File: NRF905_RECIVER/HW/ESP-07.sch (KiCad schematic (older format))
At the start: 2 parts, among them U3 ESP-07

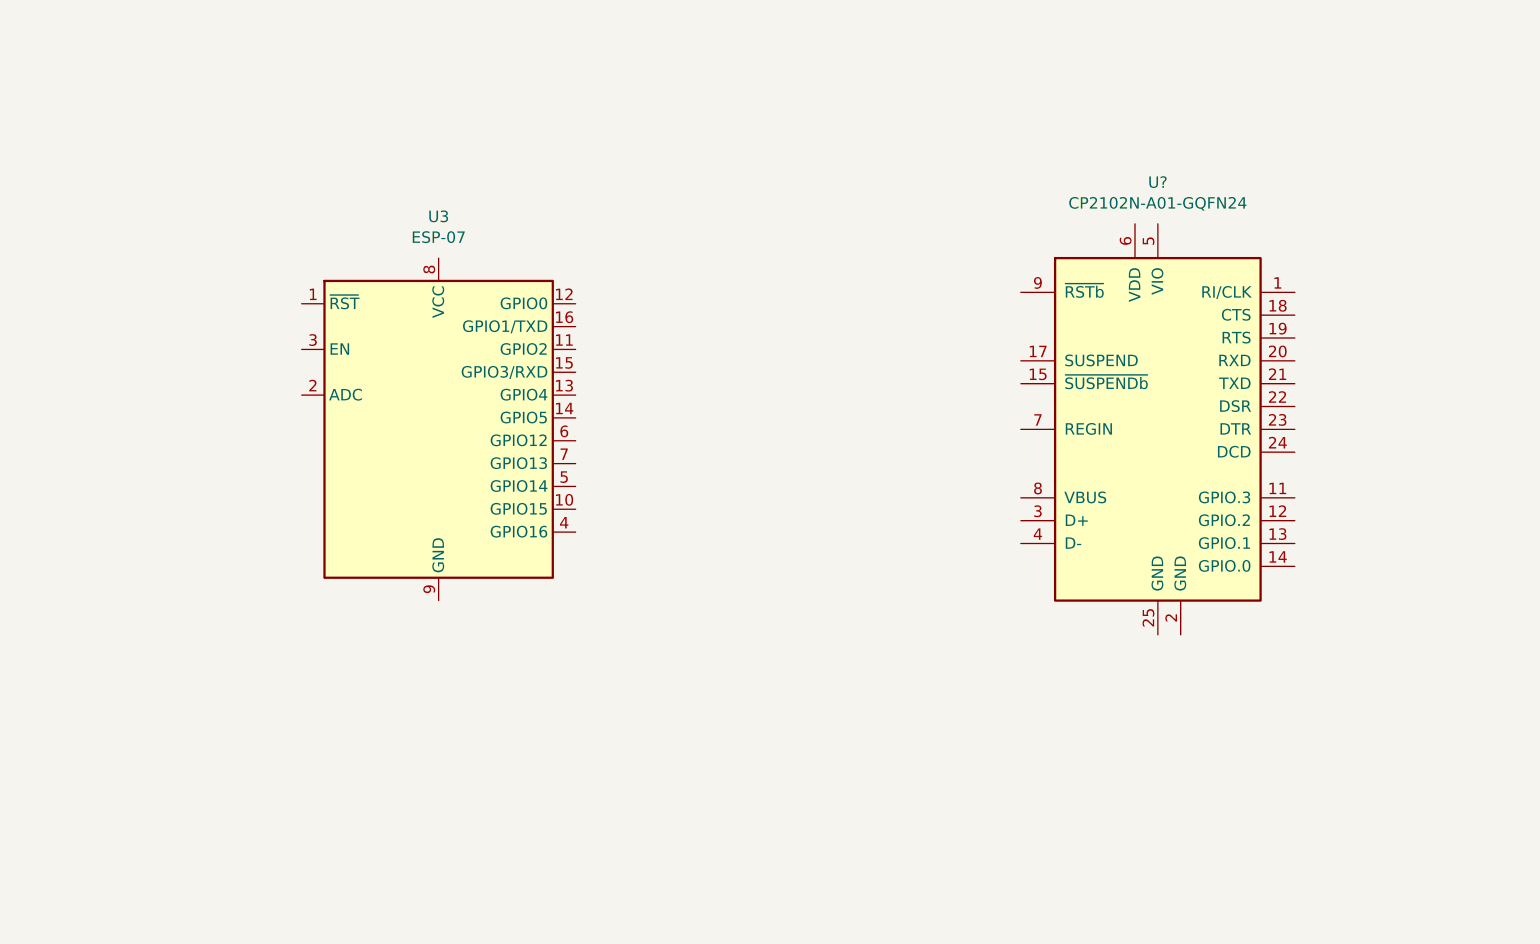
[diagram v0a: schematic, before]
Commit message: Изменена структура проека. Добавлен шаблон проекта для ESP32. Изменение в схемотехнике WIFI модуль с ESP-07 изменени на ESP32 WROVER-IB
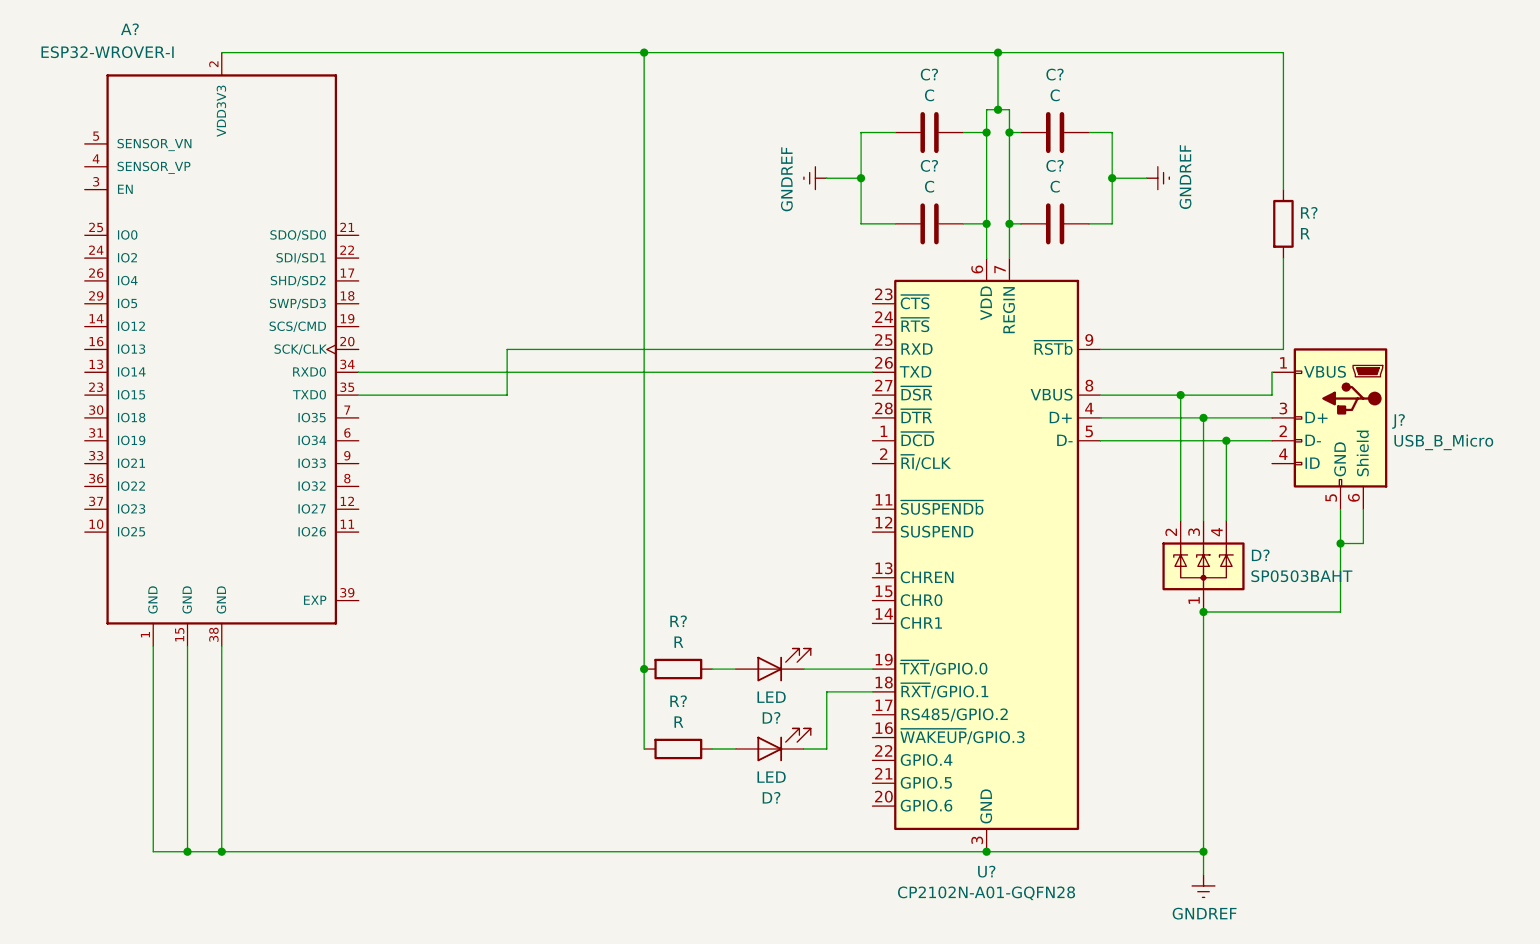
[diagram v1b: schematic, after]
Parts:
- removed U3: ESP-07, RF_Module:ESP-07, symbol RF_Module:ESP-07
- removed U?: CP2102N-A01-GQFN24, Package_DFN_QFN:QFN-24-1EP_4x4mm_P0.5mm_EP2.6x2.6mm, symbol Interface_USB:CP2102N-A01-GQFN24
- added A?: ESP32-WROVER-I, XCVR_ESP32-WROVER-I, symbol ESP32-WROVER-I:ESP32-WROVER-I
- added C? (x4): C, symbol Device:C
- added D?: SP0503BAHT, Package_TO_SOT_SMD:SOT-143, symbol Power_Protection:SP0503BAHT
- added D? (x2): LED, symbol Device:LED
- added J?: USB_B_Micro, symbol Connector:USB_B_Micro
- added R? (x3): R, symbol Device:R
- added U?: CP2102N-A01-GQFN28, Package_DFN_QFN:QFN-28-1EP_5x5mm_P0.5mm_EP3.35x3.35mm, symbol Interface_USB:CP2102N-A01-GQFN28
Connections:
- new net: D?.2 (K), J?.1 (VBUS), U?.8 (VBUS)
- new net: D?.4 (K), J?.2 (D-), U?.5 (D-)
- new net: D?.3 (K), J?.3 (D+), U?.4 (D+)
- new net: D?.1 (K), U?.18 (~RXT~/GPIO.1)
- new net: D?.1 (K), U?.19 (~TXT~/GPIO.0)
- new net: A?.35 (TXD0), U?.25 (RXD)
- new net: A?.34 (RXD0), U?.26 (TXD)
- new net: A?.2 (VDD3V3), C?.1, C?.1, C?.2, C?.2, R?.1, R?.2, R?.2, U?.6 (VDD), U?.7 (REGIN)
- new net: R?.2, U?.9 (~RSTb)
- new net: D?.2 (A), R?.1 (x2)
- new net GNDREF: A?.1 (GND), A?.15 (GND), A?.38 (GND), C?.1, C?.1, C?.2, C?.2, D?.1 (A), J?.5 (GND), J?.6 (Shield), U?.29 (GND), U?.3 (GND)
